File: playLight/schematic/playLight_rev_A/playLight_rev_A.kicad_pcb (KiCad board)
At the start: 2 copper layers, 164 x 19 mm, 21 parts, among them J1 Conn_01x01, J2 Conn_01x01, J3 Conn_01x01, J4 Conn_01x01, J5 Conn_01x01, J6 Conn_01x01, J7 Conn_01x01, J8 Conn_01x01, U1 LP5036

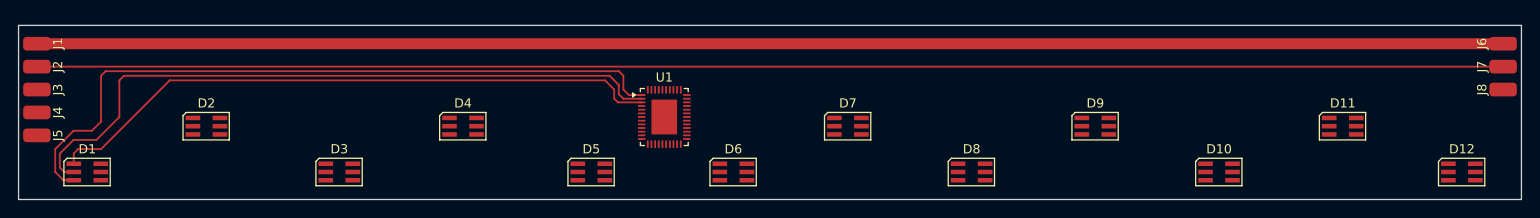
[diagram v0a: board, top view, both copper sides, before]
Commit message: added a few swaps to simplify routing
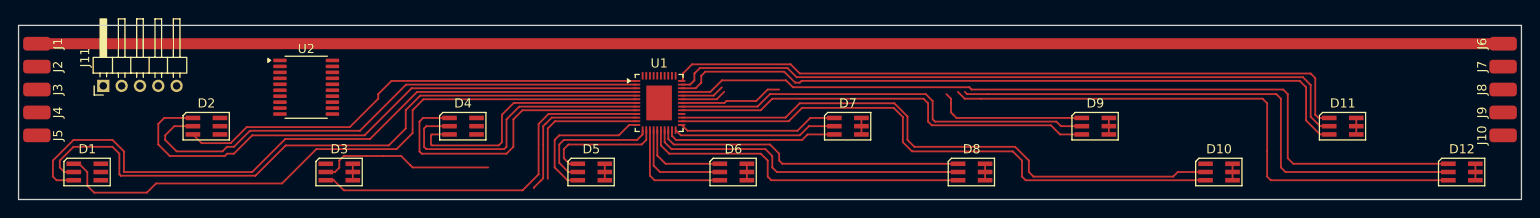
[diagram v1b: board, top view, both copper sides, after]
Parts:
- added J10: Conn_01x01, Connector_Wire:SolderWirePad_1x01_SMD_1.5x3mm, F.Cu at (212.0, 113.0)
- added J11: Conn_01x05, Connector_PinHeader_2.00mm:PinHeader_1x05_P2.00mm_Horizontal, F.Cu at (59.2, 107.6)
- added J9: Conn_01x01, Connector_Wire:SolderWirePad_1x01_SMD_1.5x3mm, F.Cu at (212.0, 110.5)
- added U2: STM32F070F6Px, Package_SO:TSSOP-20_4.4x6.5mm_P0.65mm, F.Cu at (81.4, 107.8)
- moved U1 1.64 mm to (119.9, 109.5)
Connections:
- U1 pad 1: Net-(D1-KR) -> Net-(D2-KR)
- U1 pad 10: Net-(D4-KR) -> Net-(D3-KR)
- U1 pad 11: Net-(D4-KG) -> Net-(D3-KG)
- U1 pad 12: Net-(D4-KB) -> Net-(D3-KB)
- U1 pad 19: Net-(D7-KR) -> Net-(D8-KR)
- U1 pad 2: Net-(D1-KG) -> Net-(D2-KG)
- U1 pad 20: Net-(D7-KG) -> Net-(D8-KG)
- U1 pad 21: Net-(D7-KB) -> Net-(D8-KB)
- U1 pad 22: Net-(D8-KR) -> Net-(D7-KR)
- U1 pad 23: Net-(D8-KG) -> Net-(D7-KG)
- U1 pad 24: Net-(D8-KB) -> Net-(D7-KB)
- U1 pad 25: Net-(D9-KR) -> Net-(D10-KR)
- U1 pad 26: Net-(D9-KG) -> Net-(D10-KG)
- U1 pad 27: Net-(D9-KB) -> Net-(D10-KB)
- U1 pad 28: Net-(D10-KR) -> Net-(D9-KR)
- U1 pad 29: Net-(D10-KG) -> Net-(D9-KG)
- U1 pad 3: Net-(D1-KB) -> Net-(D2-KB)
- U1 pad 30: Net-(D10-KB) -> Net-(D9-KB)
- U1 pad 31: Net-(D11-KR) -> Net-(D12-KR)
- U1 pad 32: Net-(D11-KG) -> Net-(D12-KG)
- U1 pad 33: Net-(D11-KB) -> Net-(D12-KB)
- U1 pad 34: Net-(D12-KR) -> Net-(D11-KR)
- U1 pad 35: Net-(D12-KG) -> Net-(D11-KG)
- U1 pad 36: Net-(D12-KB) -> Net-(D11-KB)
- U1 pad 4: Net-(D2-KR) -> Net-(D1-KR)
- U1 pad 5: Net-(D2-KG) -> Net-(D1-KG)
- U1 pad 6: Net-(D2-KB) -> Net-(D1-KB)
- U1 pad 7: Net-(D3-KR) -> Net-(D4-KR)
- U1 pad 8: Net-(D3-KG) -> Net-(D4-KG)
- U1 pad 9: Net-(D3-KB) -> Net-(D4-KB)
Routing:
- net Net-(J2-Pin_1): track 160.0 -> 0.00 mm
- net Net-(D12-KB): track 0.00 -> 92.1 mm
- net Net-(D11-KR): track 0.00 -> 77.0 mm
- net Net-(D11-KB): track 0.00 -> 76.6 mm
- net Net-(D11-KG): track 0.00 -> 76.5 mm
- net Net-(D12-KR): track 0.00 -> 67.2 mm
- net Net-(D12-KG): track 0.00 -> 65.6 mm
- net Net-(D10-KR): track 0.00 -> 63.7 mm
- net Net-(D10-KG): track 0.00 -> 63.6 mm
- net Net-(D2-KB): track 0.00 -> 62.1 mm
- net Net-(D2-KG): track 0.00 -> 58.9 mm
- net Net-(D2-KR): track 0.00 -> 51.9 mm
- net Net-(D9-KR): track 0.00 -> 47.0 mm
- net Net-(D9-KG): track 0.00 -> 46.8 mm
- net Net-(D3-KR): track 0.00 -> 41.0 mm
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
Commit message: added a simplified revision replaced MCU with a 2x I2C support
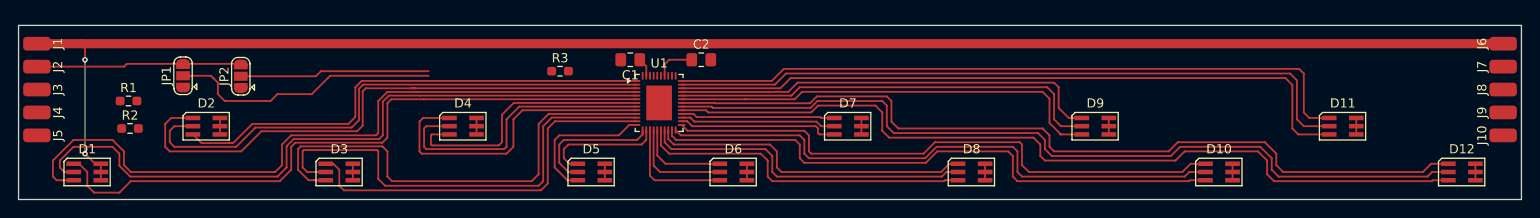
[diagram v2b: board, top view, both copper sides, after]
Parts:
- removed J11: Conn_01x05, Connector_PinHeader_2.00mm:PinHeader_1x05_P2.00mm_Horizontal
- removed U2: STM32F070F6Px, Package_SO:TSSOP-20_4.4x6.5mm_P0.65mm
- added C1: C, Capacitor_SMD:C_0805_2012Metric_Pad1.18x1.45mm_HandSolder, F.Cu at (116.8, 104.8)
- added C2: 100nF, Capacitor_SMD:C_0805_2012Metric_Pad1.18x1.45mm_HandSolder, F.Cu at (124.5, 104.8)
- added JP1: SolderJumper_3_Open, Jumper:SolderJumper-3_P1.3mm_Open_RoundedPad1.0x1.5mm, F.Cu at (68.0, 106.5)
- added JP2: SolderJumper_3_Open, Jumper:SolderJumper-3_P1.3mm_Open_RoundedPad1.0x1.5mm, F.Cu at (74.2, 106.5)
- added R1: R_US, Resistor_SMD:R_0603_1608Metric_Pad0.98x0.95mm_HandSolder, F.Cu at (62.0, 109.2)
- added R2: R_US, Resistor_SMD:R_0603_1608Metric_Pad0.98x0.95mm_HandSolder, F.Cu at (62.2, 112.2)
- added R3: R_US, Resistor_SMD:R_0603_1608Metric_Pad0.98x0.95mm_HandSolder, F.Cu at (109.1, 106.0)
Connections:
- J10 pad 1: unconnected-(J10-Pin_1-Pad1) -> Net-(J10-Pin_1)
- J4 pad 1: unconnected-(J4-Pin_1-Pad1) -> Net-(J4-Pin_1)
- J5 pad 1: unconnected-(J5-Pin_1-Pad1) -> Net-(J10-Pin_1)
- J9 pad 1: unconnected-(J9-Pin_1-Pad1) -> Net-(J4-Pin_1)
- U1 pad 22: Net-(D7-KR) -> Net-(D10-KR)
- U1 pad 23: Net-(D7-KG) -> Net-(D10-KG)
- U1 pad 24: Net-(D7-KB) -> Net-(D10-KB)
- U1 pad 25: Net-(D10-KR) -> Net-(D7-KR)
- U1 pad 26: Net-(D10-KG) -> Net-(D7-KG)
- U1 pad 27: Net-(D10-KB) -> Net-(D7-KB)
- U1 pad 28: Net-(D9-KR) -> Net-(D12-KR)
- U1 pad 29: Net-(D9-KG) -> Net-(D12-KG)
- U1 pad 30: Net-(D9-KB) -> Net-(D12-KB)
- U1 pad 31: Net-(D12-KR) -> Net-(D9-KR)
- U1 pad 32: Net-(D12-KG) -> Net-(D9-KG)
- U1 pad 33: Net-(D12-KB) -> Net-(D9-KB)
- U1 pad 38: unconnected-(U1-ADDR0-Pad38) -> Net-(JP1-C)
- U1 pad 39: unconnected-(U1-ADDR1-Pad39) -> Net-(JP2-C)
- U1 pad 41: unconnected-(U1-SDA-Pad41) -> Net-(J10-Pin_1)
- U1 pad 42: unconnected-(U1-SCL-Pad42) -> Net-(J4-Pin_1)
- U1 pad 43: unconnected-(U1-EN-Pad43) -> Net-(J2-Pin_1)
- U1 pad 44: unconnected-(U1-IREF-Pad44) -> Net-(U1-IREF)
- U1 pad 45: unconnected-(U1-VCAP-Pad45) -> Net-(U1-VCAP)
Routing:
- net Net-(D10-KB): track 0.00 -> 63.0 mm
- net Net-(JP1-C): track 0.00 -> 29.8 mm
- net Net-(D3-KB): track 15.5 -> 42.8 mm
- net Net-(J2-Pin_1): track 0.00 -> 26.6 mm
- net Net-(D12-KG): track 65.6 -> 91.1 mm
- net Net-(D12-KR): track 67.2 -> 91.1 mm
- net Net-(JP2-C): track 0.00 -> 20.7 mm
- net Net-(D1-AB): track 176.2 -> 195.9 mm, vias 0 -> 2
- net Net-(D9-KB): track 28.0 -> 47.0 mm
- net Net-(D3-KG): track 37.2 -> 50.9 mm
- net Net-(D3-KR): track 41.0 -> 52.4 mm
- net Net-(D1-KR): track 75.2 -> 78.4 mm
- net Net-(D1-KB): track 69.3 -> 71.5 mm
- net Net-(U1-VCAP): track 0.00 -> 2.05 mm
- net Net-(D1-KG): track 74.2 -> 76.1 mm
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
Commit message: finalised routing (without ground plane)
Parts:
- moved JP1 9.96 mm to (77.8, 108.2)
- moved JP2 8.42 mm to (82.5, 108.2)
- moved R2 5.55 mm to (59.8, 107.2), turned to 90 degrees
- moved R1 2.14 mm to (62.8, 107.2), turned to 90 degrees
- moved C1 1.90 mm to (115.0, 105.5)
- moved C2 0.90 mm to (124.0, 104.0)
- moved R3 0.16 mm to (109.2, 106.0), turned to 180 degrees
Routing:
- net Net-(D1-AB): track 195.9 -> 463.1 mm, vias 2 -> 11
- net Net-(J10-Pin_1): track 0.00 -> 181.2 mm, vias 0 -> 5
- net Net-(J4-Pin_1): track 0.00 -> 176.5 mm, vias 0 -> 5
- net Net-(J2-Pin_1): track 26.6 -> 184.5 mm, vias 0 -> 4
- net Net-(JP2-C): track 20.7 -> 51.3 mm, vias 0 -> 2
- net Net-(JP1-C): track 29.8 -> 56.1 mm, vias 0 -> 2
- net Net-(U1-IREF): track 0.00 -> 11.3 mm
- net Net-(D1-KR): track 78.4 -> 79.8 mm
- net Net-(U1-VCAP): track 2.05 -> 3.18 mm
- net Net-(D1-KG): track 76.1 -> 76.8 mm

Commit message: added gerbers added PDF export
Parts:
- moved R3 0.90 mm to (108.5, 105.5)
- moved C1 0.75 mm to (114.2, 105.5)
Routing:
- net GND: track 0.00 -> 38.5 mm, vias 0 -> 117
- net Net-(JP2-C): track 51.3 -> 54.3 mm
- net Net-(JP1-C): track 56.1 -> 58.2 mm
- net Net-(U1-VCAP): track 3.18 -> 3.93 mm
- net Net-(U1-IREF): track 11.3 -> 12.0 mm
- added copper zone on B.Cu, net GND
- added copper zone on F.Cu, net GND
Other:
- board text added: "+3V3"
- board text added: "+5V LED"
- board text added: "A0"
- board text added: "A1"
- board text added: "April 2026"
- board text added: "GND"
- board text added: "SCL"
- board text added: "SDA"
- board text added: "gangQin playLight"
- board text added: "rev A"

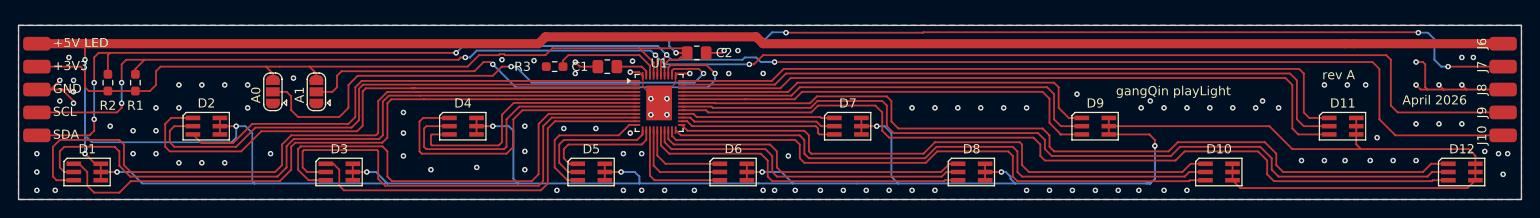
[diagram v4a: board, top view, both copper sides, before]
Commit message: added design notes in the schematic minor tweaks in the PCB generated the gerbers accordingly
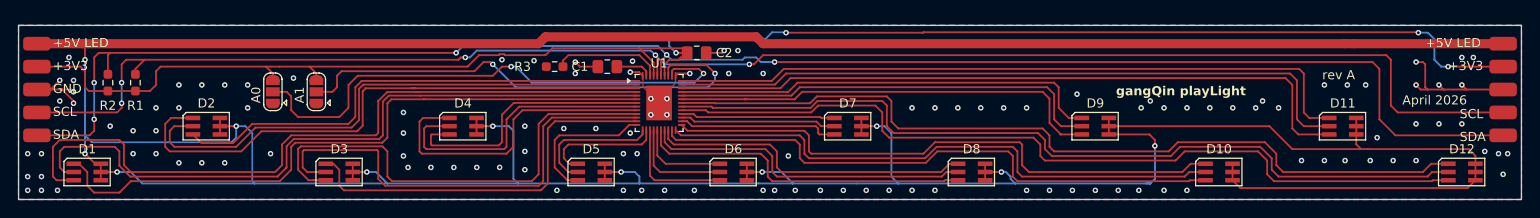
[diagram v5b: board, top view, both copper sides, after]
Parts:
- C1: value C -> 1µF
- R1, R2: value R_US -> 2.2k
- R3: value R_US -> 3.3k
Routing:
- net GND: vias 117 -> 123
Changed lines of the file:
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@@
 			(at 0 -2.3 90)
 			(layer "F.SilkS")
+			(hide yes)
 			(effects
 				(font
@@
 			)
 		)
-		(property "Value" "R_US"
+		(property "Value" "2.2k"
 			(at 0 1.43 90)
 			(layer "F.Fab")
@@
 			(at 0 -2.3 90)
 			(layer "F.SilkS")
+			(hide yes)
 			(effects
 				(font
@@
 			)
 		)
-		(property "Value" "R_US"
+		(property "Value" "3.3k"
 			(at 0 1.43 0)
 			(layer "F.Fab")
@@
 			)
 		)
-		(property "Value" "C"
+		(property "Value" "1µF"
 			(at 0 1.68 0)
 			(layer "F.Fab")
@@
 			(at 0 -2.3 90)
 			(layer "F.SilkS")
+			(hide yes)
 			(effects
 				(font
@@
 			)
 		)
-		(property "Value" "R_US"
+		(property "Value" "2.2k"
 			(at 0 1.43 90)
 			(layer "F.Fab")
@@
 			(at 0 -2.3 90)
 			(layer "F.SilkS")
+			(hide yes)
 			(effects
 				(font
@@
 			(at 0 -2.3 90)
 			(layer "F.SilkS")
+			(hide yes)
 			(effects
 				(font
@@
 		)
 	)
+	(gr_text "SCL"
+		(at 207.25 111.25 0)
+		(layer "F.SilkS")
+		(effects
+			(font
+				(size 1 1)
+				(thickness 0.125)
+			)
+			(justify left bottom)
+		)
+	)
+	(gr_text "+5V LED"
+		(at 203.5 103.5 0)
+		(layer "F.SilkS")
+		(effects
+			(font
+				(size 1 1)
+				(thickness 0.125)
+			)
+			(justify left bottom)
+		)
+	)
 	(gr_text "rev A"
 		(at 192.25 107 0)
@@
 			(font
 				(size 1 1)
+				(thickness 0.2)
+				(bold yes)
+			)
+			(justify left bottom)
+		)
+	)
+	(gr_text "SDA"
+		(at 207.25 113.75 0)
+		(layer "F.SilkS")
+		(effects
+			(font
+				(size 1 1)
 				(thickness 0.125)
 			)
@@
 		)
 	)
+	(gr_text "+3V3\n"
+		(at 206 106 0)
+		(layer "F.SilkS")
+		(effects
+			(font
+				(size 1 1)
+				(thickness 0.125)
+			)
+			(justify left bottom)
+		)
+	)
 	(segment
 		(start 69.025 112.9)
@@
 	)
 	(via
+		(at 92.5 116.5)
+		(size 0.6)
+		(drill 0.3)
+		(layers "F.Cu" "B.Cu")
+		(free yes)
+		(net 40)
+	)
+	(via
 		(at 157.5 110)
 		(size 0.6)
@@
 	)
 	(via
+		(at 51 115)
+		(size 0.6)
+		(drill 0.3)
+		(layers "F.Cu" "B.Cu")
+		(free yes)
+		(net 40)
+	)
+	(via
 		(at 118 119)
 		(size 0.6)
@@
 	)
 	(via
+		(at 97.5 116.5)
+		(size 0.6)
+		(drill 0.3)
+		(layers "F.Cu" "B.Cu")
+		(free yes)
+		(net 40)
+	)
+	(via
 		(at 172.25 119)
 		(size 0.6)
@@
 	)
 	(via
-		(at 52 115)
+		(at 52.5 115)
 		(size 0.6)
 		(drill 0.3)
@@
 	)
 	(via
+		(at 102.5 116.5)
+		(size 0.6)
+		(drill 0.3)
+		(layers "F.Cu" "B.Cu")
+		(free yes)
+		(net 40)
+	)
+	(via
 		(at 198.25 113.25)
 		(size 0.6)
@@
 	)
 	(via
-		(at 118 115)
+		(at 117.5 115)
 		(size 0.6)
 		(drill 0.3)
@@
 	)
 	(via
+		(at 52.5 119)
+		(size 0.6)
+		(drill 0.3)
+		(layers "F.Cu" "B.Cu")
+		(free yes)
+		(net 40)
+	)
+	(via
 		(at 177.5 119)
 		(size 0.6)
@@
 	)
 	(via
-		(at 52 117)
+		(at 52.5 117.5)
 		(size 0.6)
 		(drill 0.3)
@@
 	)
 	(via
-		(at 52 119)
+		(at 51 119)
 		(size 0.6)
 		(drill 0.3)
@@
 	)
 	(via
+		(at 51 117.5)
+		(size 0.6)
+		(drill 0.3)
+		(layers "F.Cu" "B.Cu")
+		(free yes)
+		(net 40)
+	)
+	(via
 		(at 185 110)
 		(size 0.6)
@@
 	)
 	(via
-		(at 95 116.75)
+		(at 95 116.5)
 		(size 0.6)
 		(drill 0.3)
@@
 	)
 	(via
-		(at 54 119)
+		(at 54.25 119)
 		(size 0.6)
 		(drill 0.3)

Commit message: changed the LED routing to pass the DRC
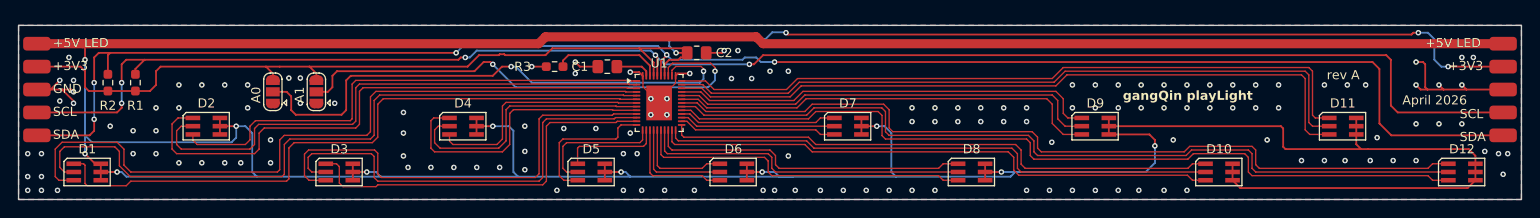
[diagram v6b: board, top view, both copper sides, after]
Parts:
- R3: value 3.3k -> 3.9k
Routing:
- net Net-(D1-AB): track 463.1 -> 455.8 mm
- net Net-(D4-KR): track 29.2 -> 25.3 mm
- net Net-(D3-KG): track 50.9 -> 48.3 mm
- net Net-(D4-KB): track 34.2 -> 31.7 mm
- net Net-(D4-KG): track 31.8 -> 29.4 mm
- net Net-(D5-KB): track 13.3 -> 10.9 mm
- net Net-(D10-KG): track 63.4 -> 61.2 mm
- net Net-(D10-KB): track 63.0 -> 60.9 mm
- net Net-(D10-KR): track 64.2 -> 62.1 mm
- net Net-(D3-KR): track 52.4 -> 50.3 mm
- net Net-(D11-KR): track 76.5 -> 78.1 mm
- net Net-(D2-KR): track 53.7 -> 55.3 mm
- net GND: track 38.5 -> 40.1 mm, vias 123 -> 147
- net Net-(D11-KG): track 76.0 -> 77.6 mm
- net Net-(D11-KB): track 75.9 -> 77.1 mm
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
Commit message: added the mounting holes required by JLCPCB
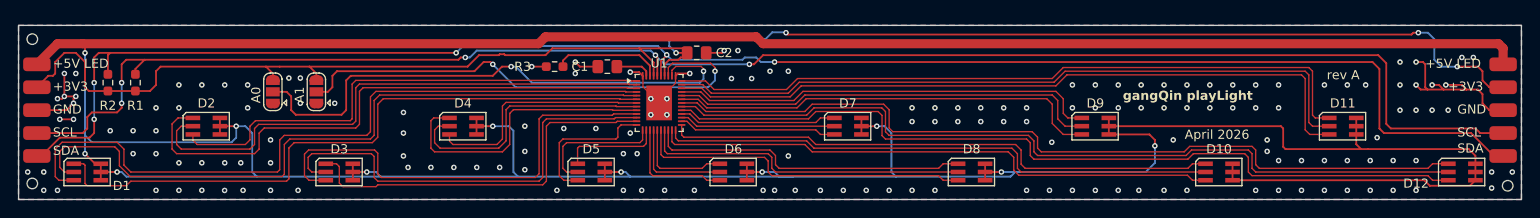
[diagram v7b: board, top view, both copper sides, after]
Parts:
- added H1: MountingHole, projectLib_playLight:JLCPCB_Tooling_Hole, F.Cu at (51.5, 102.5)
- added H2: MountingHole, projectLib_playLight:JLCPCB_Tooling_Hole, F.Cu at (51.5, 118.2)
- added H3: MountingHole, projectLib_playLight:JLCPCB_Tooling_Hole, F.Cu at (212.5, 118.5)
- moved J1 2.25 mm to (52.0, 105.2)
- moved J10 2.25 mm to (212.0, 115.2)
- moved J2 2.25 mm to (52.0, 107.8)
- moved J3 2.25 mm to (52.0, 110.2)
- moved J4 2.25 mm to (52.0, 112.8)
- moved J5 2.25 mm to (52.0, 115.2)
- moved J6 2.25 mm to (212.0, 105.2)
- moved J7 2.25 mm to (212.0, 107.8)
- moved J8 2.25 mm to (212.0, 110.2)
- moved J9 2.25 mm to (212.0, 112.8)
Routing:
- net GND: track 40.1 -> 47.8 mm, vias 147 -> 165
- net Net-(J2-Pin_1): track 184.9 -> 189.9 mm
- net Net-(J4-Pin_1): track 176.5 -> 180.0 mm
- net Net-(D1-AB): track 455.8 -> 458.5 mm
- net Net-(J10-Pin_1): track 181.5 -> 183.8 mm

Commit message: removed J connectors from BOM added LCSC refs
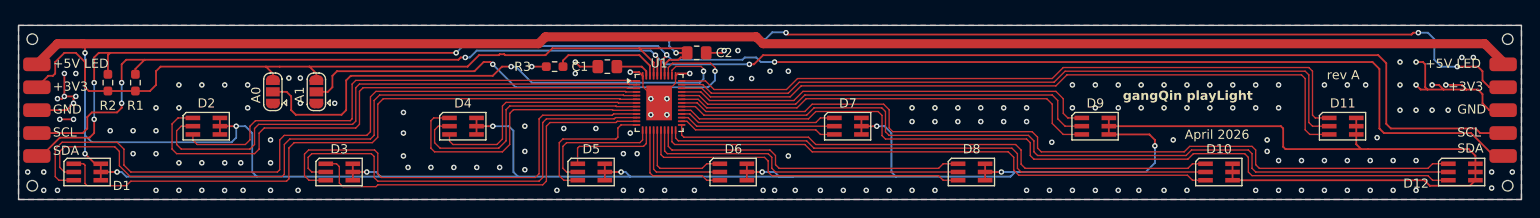
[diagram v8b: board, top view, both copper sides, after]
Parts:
- added H4: MountingHole, projectLib_playLight:JLCPCB_Tooling_Hole, F.Cu at (212.5, 102.5)
- moved H2 0.25 mm to (51.5, 118.5)
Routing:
- net Net-(D1-AB): track 458.5 -> 457.6 mm
